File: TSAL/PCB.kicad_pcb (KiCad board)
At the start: 4 copper layers, 100 x 50 mm, 63 parts, among them J1 TE 770966-2, J2 JST B04B-XASK, J3 Conn_01x02, J4 Conn_01x02, Q1 IRLZ44N, Q2 MMBT3904, Q3 IRLZ44N, U1 TL431D, U2 LMV331, U3 UCC12040DVE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

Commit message: TSAL REV3 :(
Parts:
- added C15: 100u, Capacitor_SMD:CP_Elec_6.3x7.7, F.Cu at (114.5, 79.5)
- added C8: 470p, Capacitor_SMD:C_0603_1608Metric, F.Cu at (122.7, 102.3)
- added D10: 1N4148WS, Diode_SMD:D_SOD-123, F.Cu at (124.5, 107.5)
- added D8: SSB43L, Diode_SMD:D_SMB, F.Cu at (181.8, 83.8)
- added D9: SSB43L, Diode_SMD:D_SMB, F.Cu at (170.4, 112.2)
- added JP1: SolderJumper_2_Bridged, Jumper:SolderJumper-2_P1.3mm_Bridged_RoundedPad1.0x1.5mm, F.Cu at (134.6, 91.0)
- added R20: 22k, Resistor_SMD:R_0603_1608Metric, F.Cu at (166.5, 108.5)
- added R22: 220k, Resistor_SMD:R_0603_1608Metric, F.Cu at (166.5, 111.3)
- added R23: 24k, Resistor_SMD:R_0603_1608Metric, F.Cu at (120.2, 107.5)
- added R24: 1k, Resistor_SMD:R_0603_1608Metric, F.Cu at (139.0, 94.8)
- added TP1: TestPoint, TestPoint:TestPoint_Keystone_5019_Minature, F.Cu at (115.5, 110.0)
- added TP2: TestPoint, TestPoint:TestPoint_Keystone_5019_Minature, F.Cu at (134.8, 99.5)
- added TP3: TestPoint, TestPoint:TestPoint_Keystone_5019_Minature, F.Cu at (126.5, 99.0)
- added TP4: TestPoint, TestPoint:TestPoint_Keystone_5019_Minature, F.Cu at (134.8, 94.5)
- added TP5: TestPoint, TestPoint:TestPoint_Keystone_5019_Minature, F.Cu at (134.0, 122.2)
- added TP6: TestPoint, TestPoint:TestPoint_Keystone_5019_Minature, F.Cu at (129.8, 109.0)
- added U6: LF50_TO252, Package_TO_SOT_SMD:TO-252-2, F.Cu at (137.8, 83.2)
- C1: value 100n -> 220n
- C2: value 100u -> 0.1u
- D4: value AES2JF-HF -> STTH1R06A; footprint KiCADv6:CR_SMAF_CIP -> Diode_SMD:D_SMA
- L1: footprint Inductor_SMD:L_1008_2520Metric -> Inductor_SMD:L_12x12mm_H8mm
- R16: value 22k -> 220k
- R17, R18: value 5k -> 20k
- R6: value 2.2k -> 1k
- R7: value 100k -> 10k
- moved R7 35.6 mm to (175.2, 84.5)
- moved D4 21.8 mm to (115.2, 87.5)
- moved L1 19.2 mm to (124.2, 89.5), turned to 90 degrees
- moved C2 13.4 mm to (133.2, 85.8), turned to 90 degrees
- moved H1 13.1 mm to (105.0, 80.0)
- moved R29 12.6 mm to (131.4, 131.0)
- moved L2 12.5 mm to (116.0, 98.5)
- moved D1 12.4 mm to (135.0, 128.0), turned to 90 degrees
- moved H2 11.3 mm to (195.0, 80.0)
- moved R28 11.2 mm to (126.0, 131.0), turned to 0 degrees
- moved C9 10.2 mm to (107.6, 92.8), turned to 180 degrees
- moved R4 10.1 mm to (121.0, 129.0), turned to -90 degrees
- moved R5 9.78 mm to (139.0, 128.0), turned to 90 degrees
- moved C11 8.90 mm to (140.0, 91.3)
- moved U2 7.49 mm to (135.4, 106.2)
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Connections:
- C2 pad 1: +5V -> Net-(D6-A)
- D6 pad 2: +5V -> Net-(D6-A)
- L1 pad 2: +5V -> Net-(D6-A)
- R7 pad 1: Net-(R16-Pad1) -> Net-(D8-K)
- R7 pad 2: GND -> Net-(R16-Pad1)
- U4 pad 3: Net-(R16-Pad1) -> GND
- U4 pad 4: +5V@GLV -> Net-(R16-Pad1)
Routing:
- net Net-(R16-Pad1): track 8.89 -> 61.0 mm, vias 0 -> 2
- net Net-(D6-A): track 0.00 -> 41.5 mm
- net Net-(D1-K): track 7.66 -> 32.5 mm
- net Net-(D4-K): track 21.8 -> 3.22 mm, vias 0 -> 16
- net Net-(U2-+): track 3.01 -> 20.4 mm
- net Net-(U7-FB): track 5.74 -> 22.2 mm
- net TS+: track 30.9 -> 46.7 mm
- net TS-: track 55.9 -> 69.5 mm, vias 12 -> 62
- net Net-(U7-VCC): track 1.94 -> 14.5 mm, vias 0 -> 2
- net +5V@GLV: track 31.7 -> 42.0 mm
- net Net-(D10-A): track 7.24 -> 17.3 mm
- net Net-(U7-DRAIN): track 9.46 -> 0.42 mm, vias 0 -> 12
- net /Ext-LED-RED: track 42.3 -> 51.3 mm
- net +12V: track 16.5 -> 23.8 mm
- net +5V: track 25.9 -> 31.6 mm
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- added copper zone on B.Cu, net Net-(D4-K)
- added copper zone on F.Cu, net Net-(D4-K)
- added copper zone on In1.Cu, net Net-(D4-K)
- added copper zone on In2.Cu, net Net-(D4-K)
- added copper zone on F.Cu, net Net-(D6-A)
- added copper zone on B.Cu, net Net-(U7-DRAIN)
- added copper zone on F.Cu, net Net-(U7-DRAIN)
- added copper zone on In1.Cu, net Net-(U7-DRAIN)
- added copper zone on In2.Cu, net Net-(U7-DRAIN)
- added copper zone on B.Cu, net TS-
- added copper zone on F.Cu, net TS-
- added copper zone on In2.Cu, net TS-
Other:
- board size 100 x 50 mm -> 100 x 60 mm
- board text added: "Bronco Racing TSAL + Voltage Indicator REV 3"
- board text added: "TSAL REV 3 2024 J. Iwick J. LeFevre"
- board text removed: "Bronco Racing TSAL + Voltage Indicator Rev 2"
- board text removed: "Josh Iwick Feb 2023"
- board text removed: "TS+"
- board text removed: "TS-"
- board text removed: "TSAL V2 J. Iwick 2024"

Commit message: TSAL V3 Minor changes
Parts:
- H1, H2, H3, H4: footprint MountingHole:MountingHole_4mm -> MountingHole:MountingHole_3.2mm_M3
- moved D6 0.50 mm to (129.0, 104.6)
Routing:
- net Net-(D10-A): track 17.3 -> 17.8 mm
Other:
- board text added: "TS+"
- board text added: "TS-"

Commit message: Minor changes once again
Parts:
- L2: footprint Inductor_SMD:L_1008_2520Metric -> Inductor_SMD:L_1210_3225Metric
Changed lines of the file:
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@@
     )
   )
-  (footprint "Inductor_SMD:L_1008_2520Metric" (layer "F.Cu")
+  (footprint "Inductor_SMD:L_1210_3225Metric" (layer "F.Cu")
     (at 116 98.5 90)
-    (descr "Inductor SMD 1008 (2520 Metric), square (rectangular) end terminal, IPC_7351 nominal, (Body size source: https://ecsxtal.com/store/pdf/ECS-MPI2520-SMD-POWER-INDUCTOR.pdf), generated with kicad-footprint-generator")
+    (descr "Inductor SMD 1210 (3225 Metric), square (rectangular) end terminal, IPC_7351 nominal, (Body size source: http://www.tortai-tech.com/upload/download/2011102023233369053.pdf), generated with kicad-footprint-generator")
     (tags "inductor")
     (property "Sheetfile" "PCB.kicad_sch")
@@
     (property "ki_keywords" "inductor choke coil reactor magnetic")
     (attr smd)
-    (fp_text reference "L2" (at 0 -2.05 90) (layer "F.SilkS")
+    (fp_text reference "L2" (at 0 -2.28 90) (layer "F.SilkS")
         (effects (font (size 1 1) (thickness 0.15)))
     )
-    (fp_text value "1m" (at 0 2.05 90) (layer "F.Fab")
+    (fp_text value "1m" (at 0 2.28 90) (layer "F.Fab")
         (effects (font (size 1 1) (thickness 0.15)))
     )
     (fp_text user "${REFERENCE}" (at 0 0 90) (layer "F.Fab")
-        (effects (font (size 0.62 0.62) (thickness 0.09)))
+        (effects (font (size 0.8 0.8) (thickness 0.12)))
     )
-    (fp_line (start -0.261252 -1.11) (end 0.261252 -1.11)
+    (fp_line (start -0.602064 -1.36) (end 0.602064 -1.36)
       (stroke (width 0.12) (type solid)) (layer "F.SilkS"))
-    (fp_line (start -0.261252 1.11) (end 0.261252 1.11)
+    (fp_line (start -0.602064 1.36) (end 0.602064 1.36)
       (stroke (width 0.12) (type solid)) (layer "F.SilkS"))
-    (fp_line (start -1.95 -1.35) (end 1.95 -1.35)
+    (fp_line (start -2.28 -1.58) (end 2.28 -1.58)
       (stroke (width 0.05) (type solid)) (layer "F.CrtYd"))
-    (fp_line (start -1.95 1.35) (end -1.95 -1.35)
+    (fp_line (start -2.28 1.58) (end -2.28 -1.58)
       (stroke (width 0.05) (type solid)) (layer "F.CrtYd"))
-    (fp_line (start 1.95 -1.35) (end 1.95 1.35)
+    (fp_line (start 2.28 -1.58) (end 2.28 1.58)
       (stroke (width 0.05) (type solid)) (layer "F.CrtYd"))
-    (fp_line (start 1.95 1.35) (end -1.95 1.35)
+    (fp_line (start 2.28 1.58) (end -2.28 1.58)
       (stroke (width 0.05) (type solid)) (layer "F.CrtYd"))
-    (fp_line (start -1.25 -1) (end 1.25 -1)
+    (fp_line (start -1.6 -1.25) (end 1.6 -1.25)
       (stroke (width 0.1) (type solid)) (layer "F.Fab"))
-    (fp_line (start -1.25 1) (end -1.25 -1)
+    (fp_line (start -1.6 1.25) (end -1.6 -1.25)
       (stroke (width 0.1) (type solid)) (layer "F.Fab"))
-    (fp_line (start 1.25 -1) (end 1.25 1)
+    (fp_line (start 1.6 -1.25) (end 1.6 1.25)
       (stroke (width 0.1) (type solid)) (layer "F.Fab"))
-    (fp_line (start 1.25 1) (end -1.25 1)
+    (fp_line (start 1.6 1.25) (end -1.6 1.25)
       (stroke (width 0.1) (type solid)) (layer "F.Fab"))
-    (pad "1" smd roundrect (at -1.075 0 90) (size 1.25 2.2) (layers "F.Cu" "F.Paste" "F.Mask") (roundrect_rratio 0.2)
+    (pad "1" smd roundrect (at -1.4 0 90) (size 1.25 2.65) (layers "F.Cu" "F.Paste" "F.Mask") (roundrect_rratio 0.2)
       (net 25 "TS+") (pinfunction "1") (pintype "passive"))
-    (pad "2" smd roundrect (at 1.075 0 90) (size 1.25 2.2) (layers "F.Cu" "F.Paste" "F.Mask") (roundrect_rratio 0.2)
+    (pad "2" smd roundrect (at 1.4 0 90) (size 1.25 2.65) (layers "F.Cu" "F.Paste" "F.Mask") (roundrect_rratio 0.2)
       (net 11 "Net-(U7-DRAIN)") (pinfunction "2") (pintype "passive"))
-    (model "${KICAD6_3DMODEL_DIR}/Inductor_SMD.3dshapes/L_1008_2520Metric.wrl"
+    (model "${KICAD6_3DMODEL_DIR}/Inductor_SMD.3dshapes/L_1210_3225Metric.wrl"
       (offset (xyz 0 0 0))
       (scale (xyz 1 1 1))
@@
   (segment (start 115 122.07) (end 114.32 122.07) (width 1) (layer "F.Cu") (net 25))
   (segment (start 104.75 123.75) (end 112.64 123.75) (width 1) (layer "F.Cu") (net 25))
-  (segment (start 112 104.6) (end 116 100.6) (width 1) (layer "F.Cu") (net 25))
-  (segment (start 116 100.6) (end 116 100.05) (width 1) (layer "F.Cu") (net 25))
+  (segment (start 112 103.9) (end 116 99.9) (width 1) (layer "F.Cu") (net 25))
   (segment (start 120.5325 122.07) (end 121 122.5375) (width 1) (layer "F.Cu") (net 25))
   (segment (start 103.25 122.25) (end 104.75 123.75) (width 1) (layer "F.Cu") (net 25))
+  (segment (start 112 104.6) (end 112 103.9) (width 1) (layer "F.Cu") (net 25))
   (segment (start 177.5 106.425) (end 177.5 106.1533) (width 0.25) (layer "F.Cu") (net 26))
   (segment (start 177.4499 104.9934) (end 177.5049 105.0484) (width 0.25) (layer "F.Cu") (net 26))

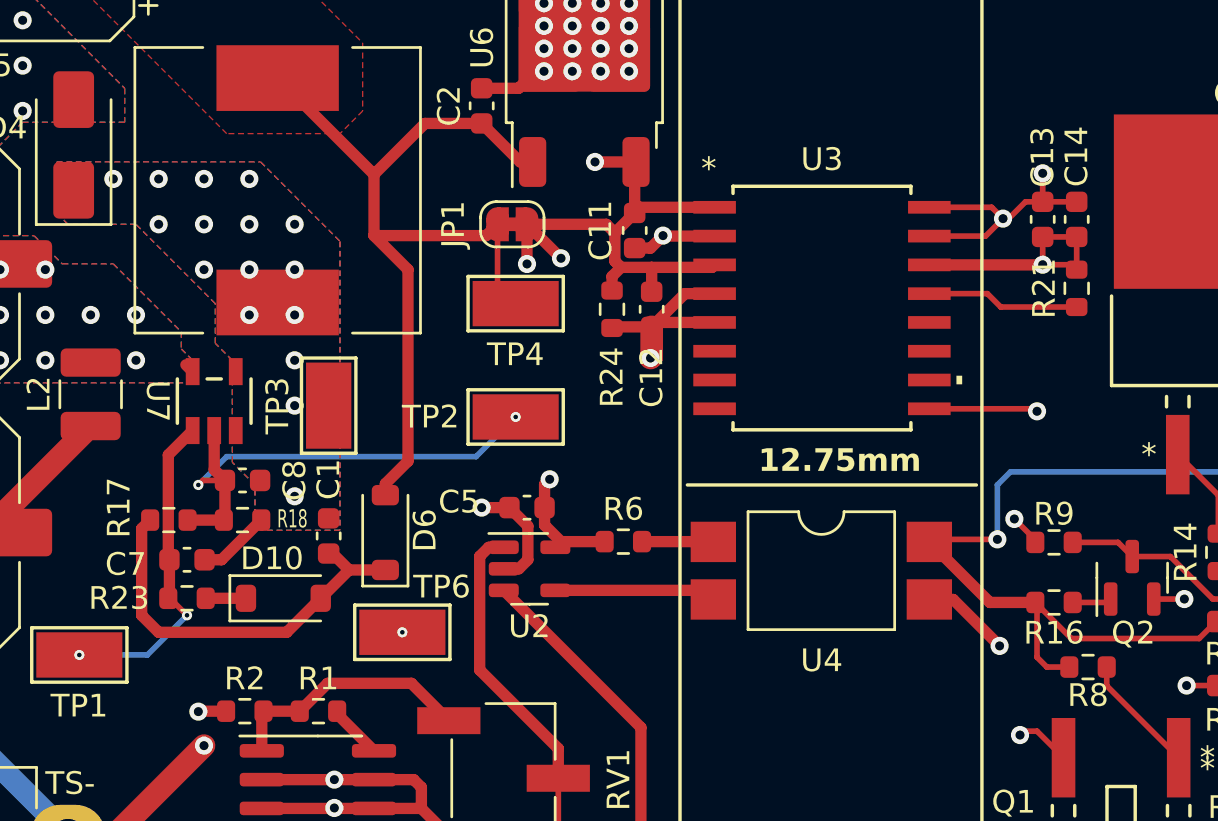
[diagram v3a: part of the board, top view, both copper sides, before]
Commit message: Edit to PCB due to footprint change
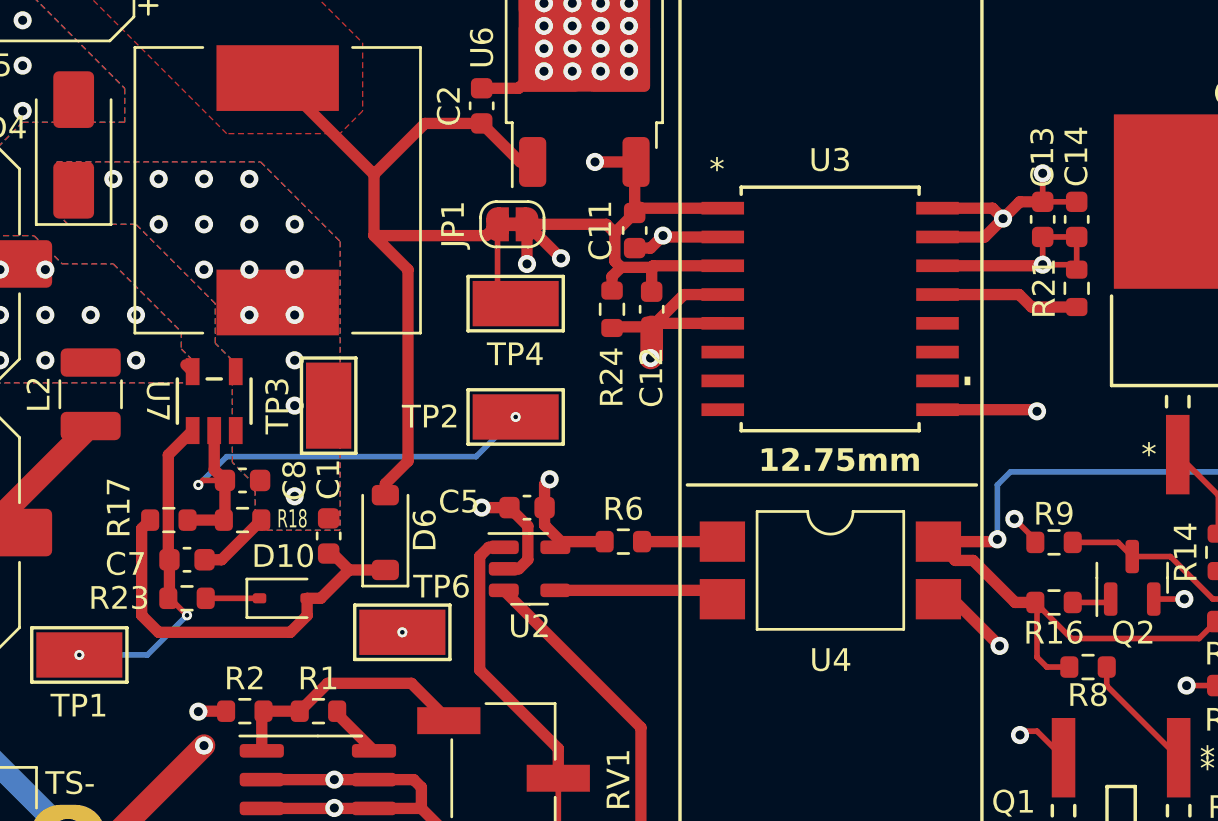
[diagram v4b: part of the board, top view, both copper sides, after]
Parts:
- C3, C5, C6: value 100n -> 0.1u
- D10: footprint Diode_SMD:D_SOD-123 -> Diode_SMD:D_SOD-323
- moved U4 0.40 mm to (148.6, 106.3)
- moved U3 0.36 mm to (148.6, 94.7)
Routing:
- net TS-: track 69.5 -> 70.5 mm
- net +5V: track 31.6 -> 32.6 mm
- net Net-(U2-Pad4): track 7.14 -> 8.10 mm
- net Net-(D10-K): track 1.77 -> 2.38 mm
- net Net-(R16-Pad1): track 61.0 -> 60.4 mm
